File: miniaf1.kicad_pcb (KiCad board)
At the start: 2 copper layers, 86.3 x 53.3 mm, 49 parts, among them J1 AF IN, J2 Barrel_Jack, J3 AF OUT, SW1 SW_Rotary3x4, U1 LM348, U2 LM386

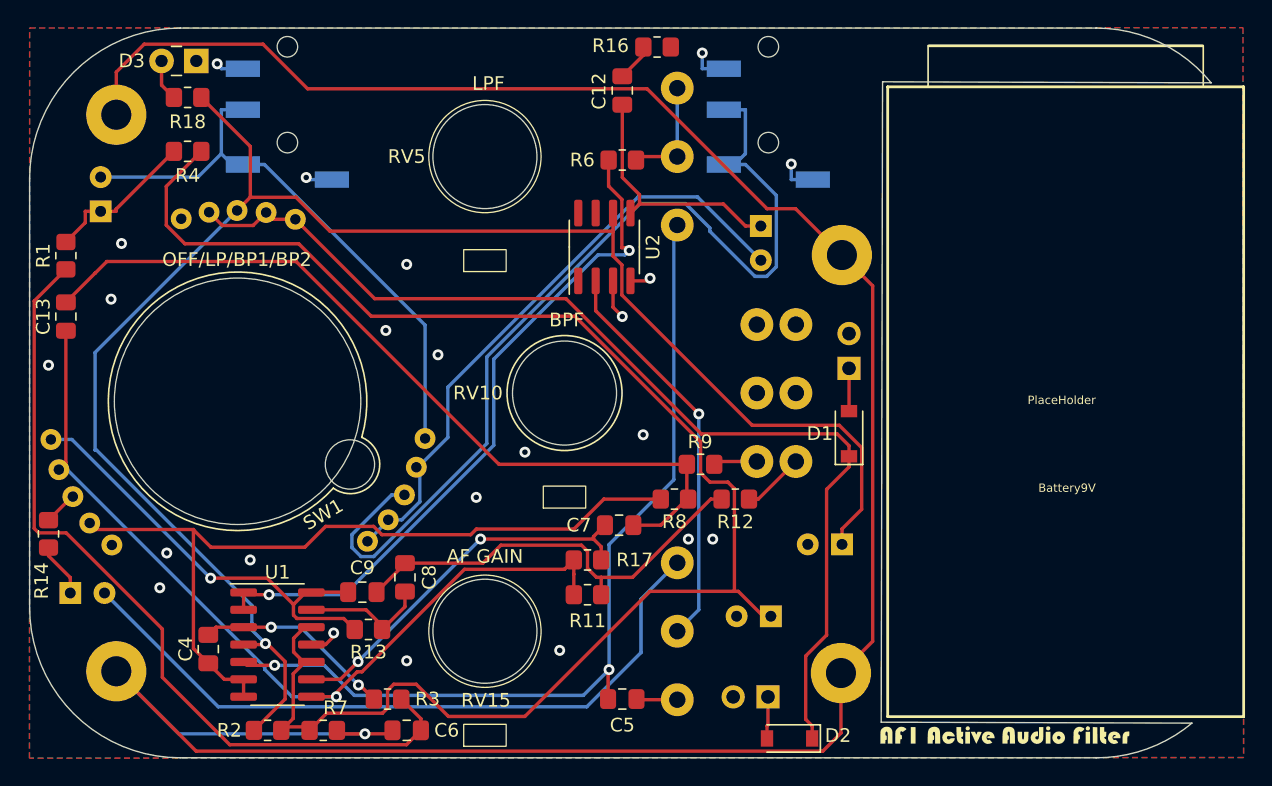
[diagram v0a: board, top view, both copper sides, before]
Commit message: refresh WH148 footprint, make more room for easy install
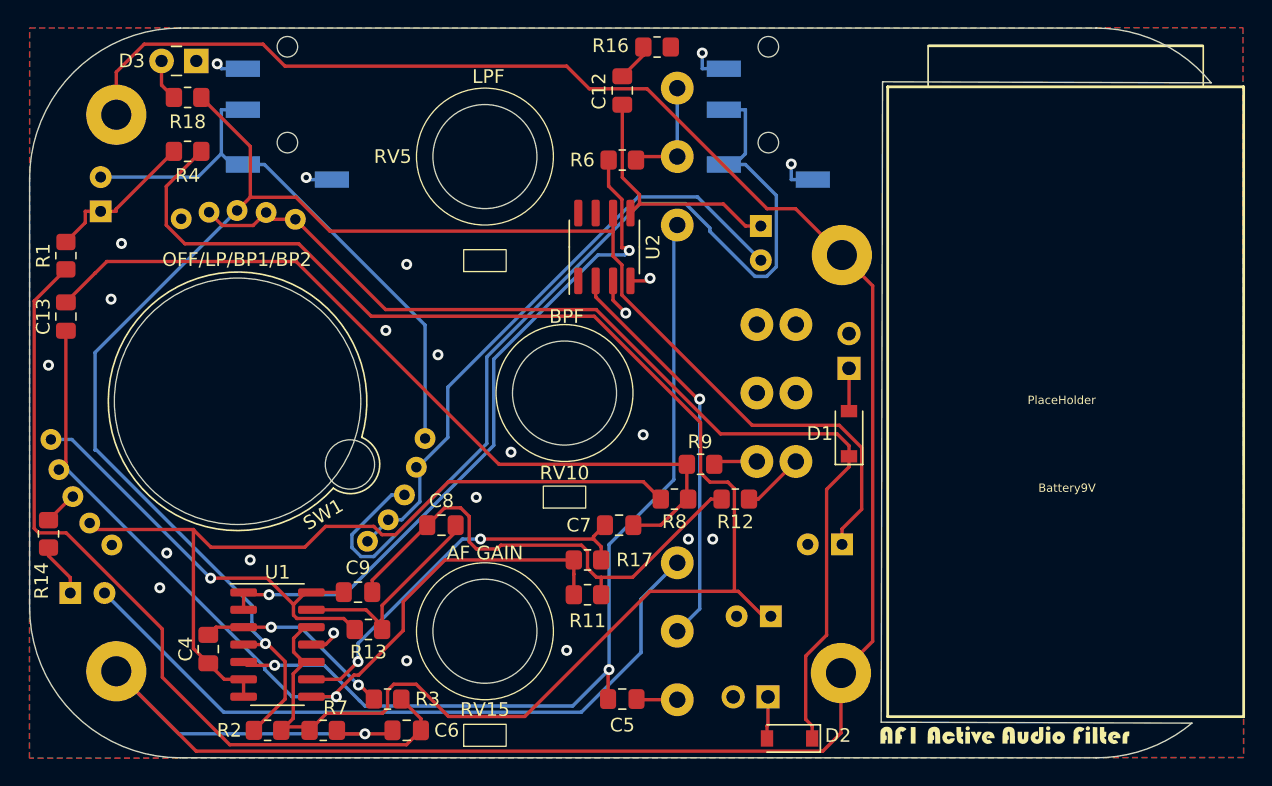
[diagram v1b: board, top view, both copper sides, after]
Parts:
- moved C8 4.65 mm to (110.0, 92.7), turned to 180 degrees
- moved C9 0.32 mm to (103.9, 97.6)
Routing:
- net Net-(C8-Pad1): track 9.39 -> 15.8 mm
- net Net-(C8-Pad2): track 32.0 -> 36.4 mm
- net Net-(C13-Pad2): track 63.6 -> 64.8 mm
- net Net-(C4-Pad2): track 59.0 -> 60.0 mm
- net +VCCM: track 118.7 -> 119.5 mm
- net Net-(C7-Pad1): track 28.0 -> 28.8 mm
- net Net-(C5-Pad2): track 65.2 -> 65.8 mm

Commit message: add enclosure comment in PCB layout for drill
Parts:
- added REF**: ALTOIDS_round_94mmx59mmx22mm_hole_2.0mm, CraftsmanICs:ALTOIDS_round_rectangle_89mmx54mmx19mm_no_holes_with_outerbound, F.Cu at (124.3, 83.1)
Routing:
- net GNDREF: vias 24 -> 26
